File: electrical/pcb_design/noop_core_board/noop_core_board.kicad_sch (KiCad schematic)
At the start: 1 part

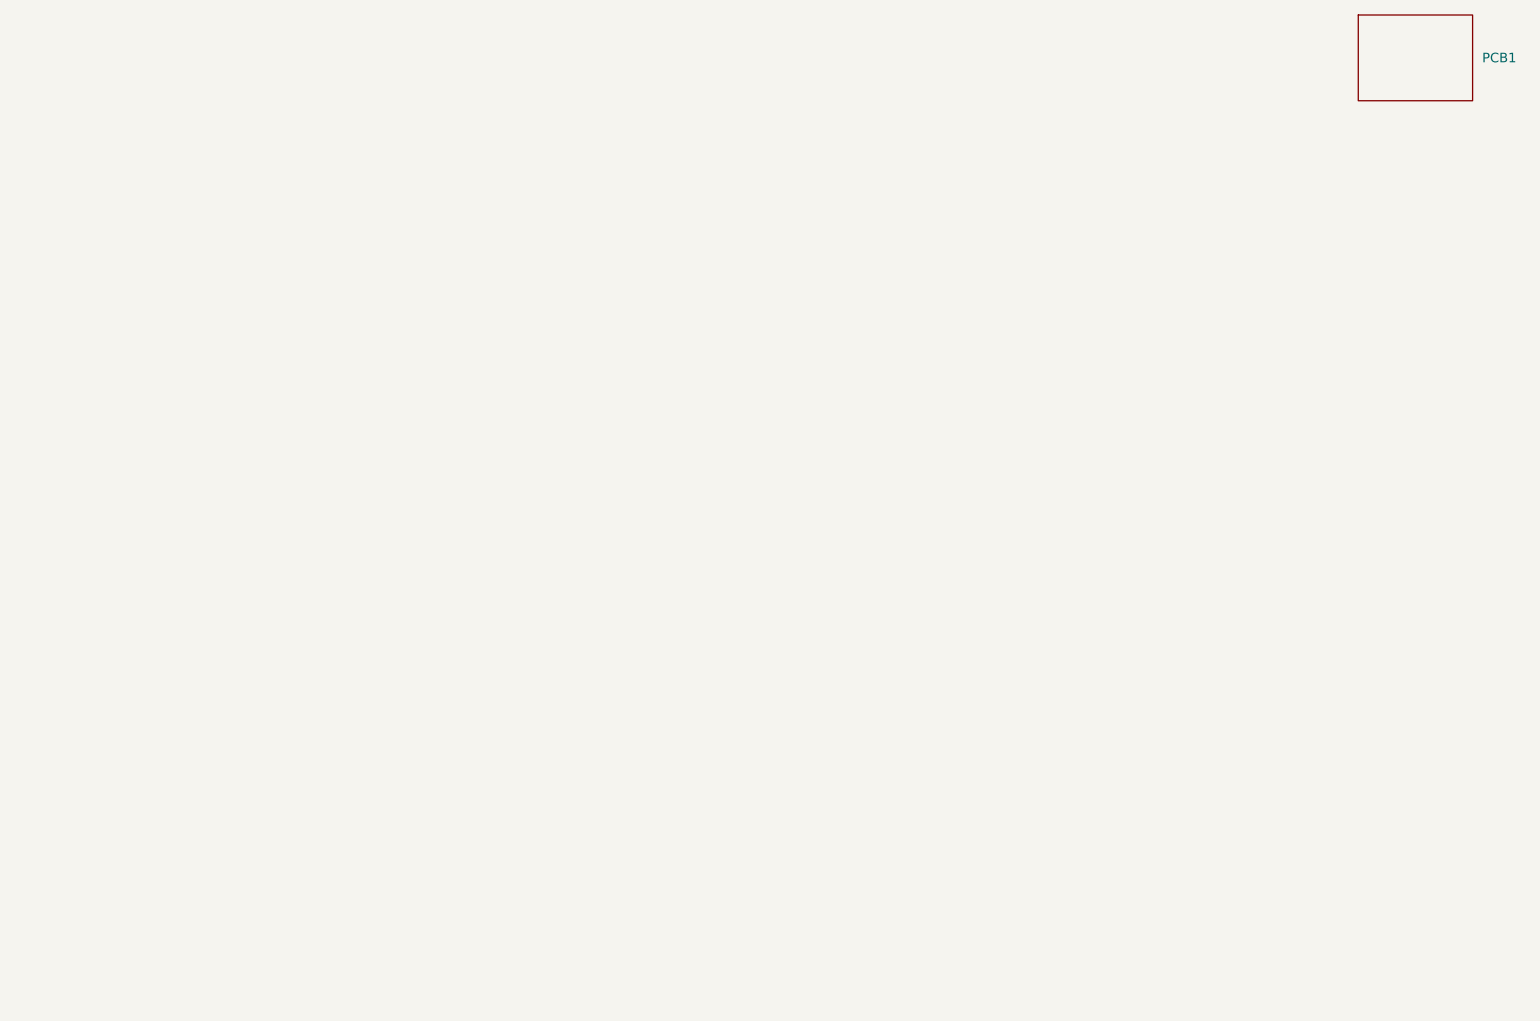
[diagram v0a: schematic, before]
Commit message: Added edge fingers to noop core board. Updated core board symbol and footprint to match. Completed first layout; still need to audit connections to other boards for consistency.
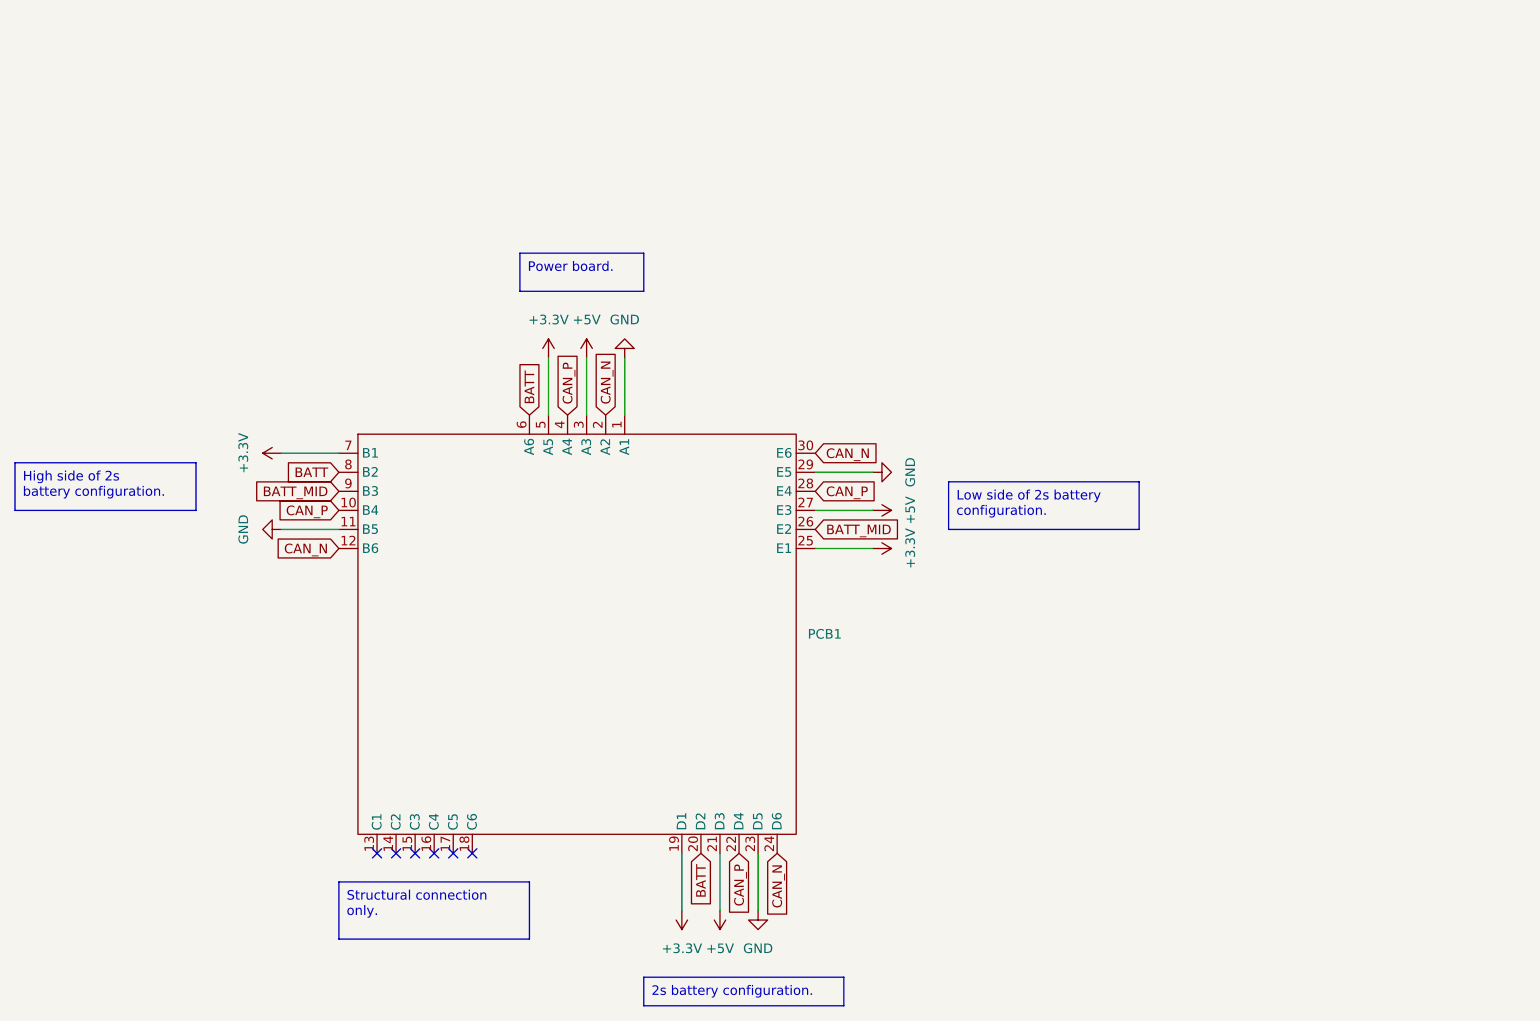
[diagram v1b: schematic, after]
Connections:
- new net +3.3V: PCB1.19 (D1), PCB1.25 (E1), PCB1.5 (A5), PCB1.7 (B1)
- new net +5V: PCB1.21 (D3), PCB1.27 (E3), PCB1.3 (A3)
- new net BATT: PCB1.20 (D2), PCB1.6 (A6), PCB1.8 (B2)
- new net BATT_MID: PCB1.26 (E2), PCB1.9 (B3)
- new net CAN_N: PCB1.12 (B6), PCB1.2 (A2), PCB1.24 (D6), PCB1.30 (E6)
- new net CAN_P: PCB1.10 (B4), PCB1.22 (D4), PCB1.28 (E4), PCB1.4 (A4)
- new net GND: PCB1.1 (A1), PCB1.11 (B5), PCB1.23 (D5), PCB1.29 (E5)
- no-connect marks 0 -> 6

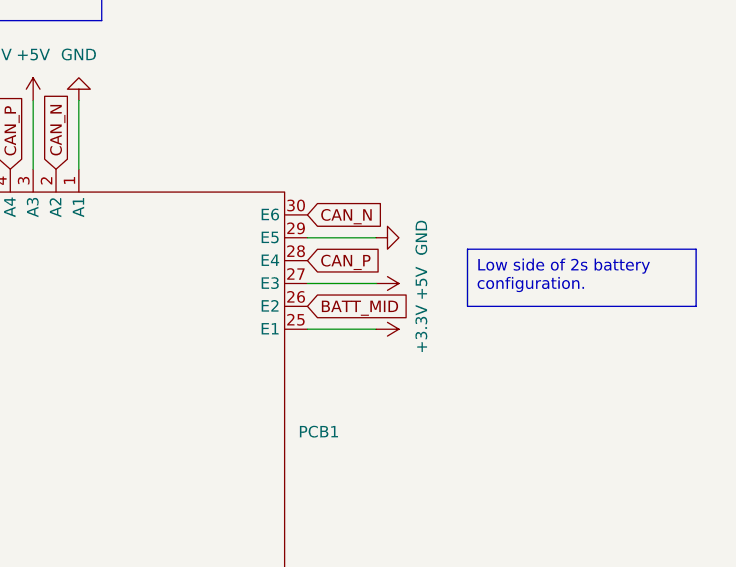
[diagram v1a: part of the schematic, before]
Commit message: Further attempts to fix the shape of the interior core boards. Plus, updates to the electrical connections on one connector.
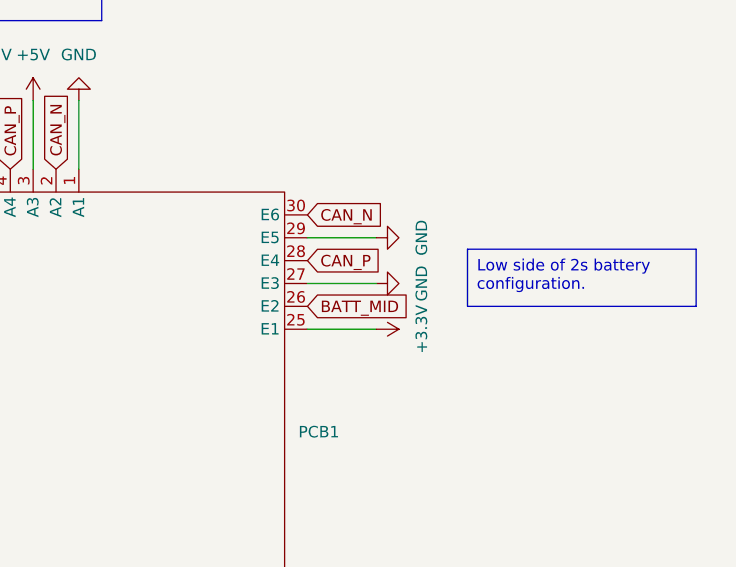
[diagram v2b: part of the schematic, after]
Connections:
- net +5V: no longer PCB1.27 (E3)
- net GND: now also PCB1.27 (E3)
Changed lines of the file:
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@@
-    )
-  )
-  (symbol (lib_id "power:+5V") (at 177.8 85.09 270) (unit 1)
-    (in_bom yes) (on_board yes) (dnp no) (fields_autoplaced)
-    (property "Reference" "#PWR011" (at 173.99 85.09 0)
-      (effects (font (size 1.27 1.27)) hide)
-    )
-    (property "Value" "+5V" (at 182.88 85.09 0)
-      (effects (font (size 1.27 1.27)))
-    )
-    (property "Footprint" "" (at 177.8 85.09 0)
-      (effects (font (size 1.27 1.27)) hide)
-    )
-    (property "Datasheet" "" (at 177.8 85.09 0)
-      (effects (font (size 1.27 1.27)) hide)
-    )
-    (pin "1")
-    (instances
-      (project "noop_core_board"
-        (path "/476cf7fd-4f82-4468-99c1-e027b17f5088"
-          (reference "#PWR011") (unit 1)
-        )
-      )
     )
   )
@@
         )
       )
+    )
+  )
+  (symbol (lib_id "power:GND") (at 177.8 85.09 90) (unit 1)
+    (in_bom yes) (on_board yes) (dnp no) (fields_autoplaced)
+    (property "Reference" "#PWR011" (at 184.15 85.09 0)
+      (effects (font (size 1.27 1.27)) hide)
+    )
+    (property "Value" "GND" (at 182.88 85.09 0)
+      (effects (font (size 1.27 1.27)))
+    )
+    (property "Footprint" "" (at 177.8 85.09 0)
+      (effects (font (size 1.27 1.27)) hide)
+    )
+    (property "Datasheet" "" (at 177.8 85.09 0)
+      (effects (font (size 1.27 1.27)) hide)
+    )
+    (pin "1")
+    (instances
+      (project "noop_core_board"
+        (path "/476cf7fd-4f82-4468-99c1-e027b17f5088"
+          (reference "#PWR011") (unit 1)
+        )
+      )
